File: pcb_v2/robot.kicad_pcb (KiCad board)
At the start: 2 copper layers, 34.9 x 72.4 mm, 28 parts, among them J1 M1 PWR, J11 MB CTRL, J12 MA CTRL, J2 M2 PWR, J3 Power Connector, J4 BATT, J5 TB6612_Motor_Driver, J7 PWR, Q1 2N3904, Q2 2N3904, U2 L7805, U3 L78L33_TO92

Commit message: SMB, 10 Dec 19, updated 3d print files.
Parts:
- removed the ? at (123.2, 35.6)
- added ?: , , F.Cu at (102.9, 27.9)
- added ?: , , F.Cu at (96.5, 27.9)
- added D2: LED, LED_THT:LED_D3.0mm, F.Cu at (99.1, 22.9)
- added Q3: 2N3906, Package_TO_SOT_THT:TO-92_Inline_Wide, F.Cu at (108.0, 22.9)
- added R2: 10k, Resistor_THT:R_Axial_DIN0207_L6.3mm_D2.5mm_P10.16mm_Horizontal, F.Cu at (102.9, 27.9)
- added R7: 13k, Resistor_THT:R_Axial_DIN0207_L6.3mm_D2.5mm_P10.16mm_Horizontal, F.Cu at (118.1, 27.9)
- added R8: 1k, Resistor_THT:R_Axial_DIN0207_L6.3mm_D2.5mm_P10.16mm_Horizontal, F.Cu at (118.1, 22.9)
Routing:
- net GND: track 139.6 -> 175.4 mm
- net +5V: track 96.6 -> 127.1 mm
- net Net-(D2-Pad2): track 0.00 -> 28.8 mm
- net Net-(Q3-Pad2): track 0.00 -> 11.2 mm
- net +BATT: track 74.8 -> 83.3 mm
- net Net-(Q3-Pad3): track 0.00 -> 5.08 mm
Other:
- board size 34.9 x 72.4 mm -> 34.9 x 82.5 mm
- board text added: "13k"
- board text added: "1k"
- board text added: "Beyer (c) 2019"
- board text removed: "Walchko (c) 2018"

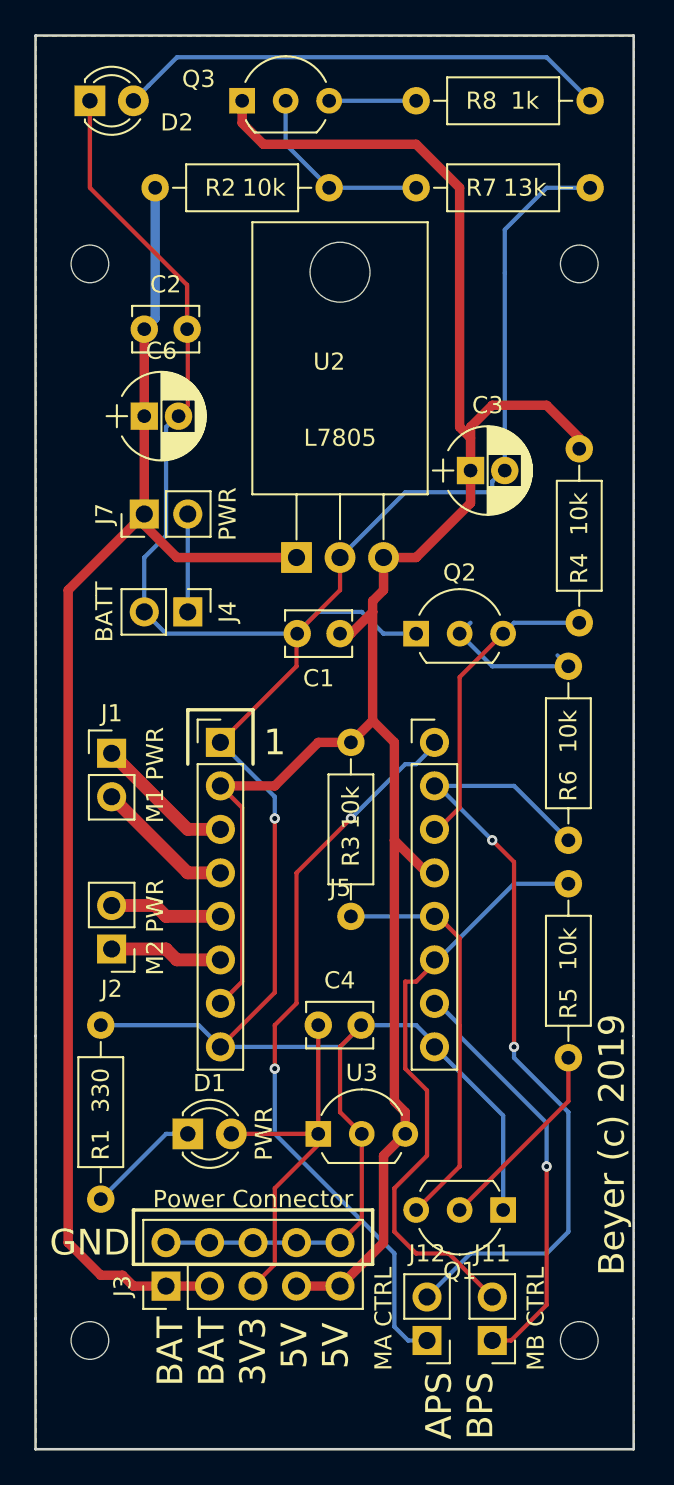
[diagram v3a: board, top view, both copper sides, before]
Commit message: SMB, 28 Apr 2020, Updated PCB v2.
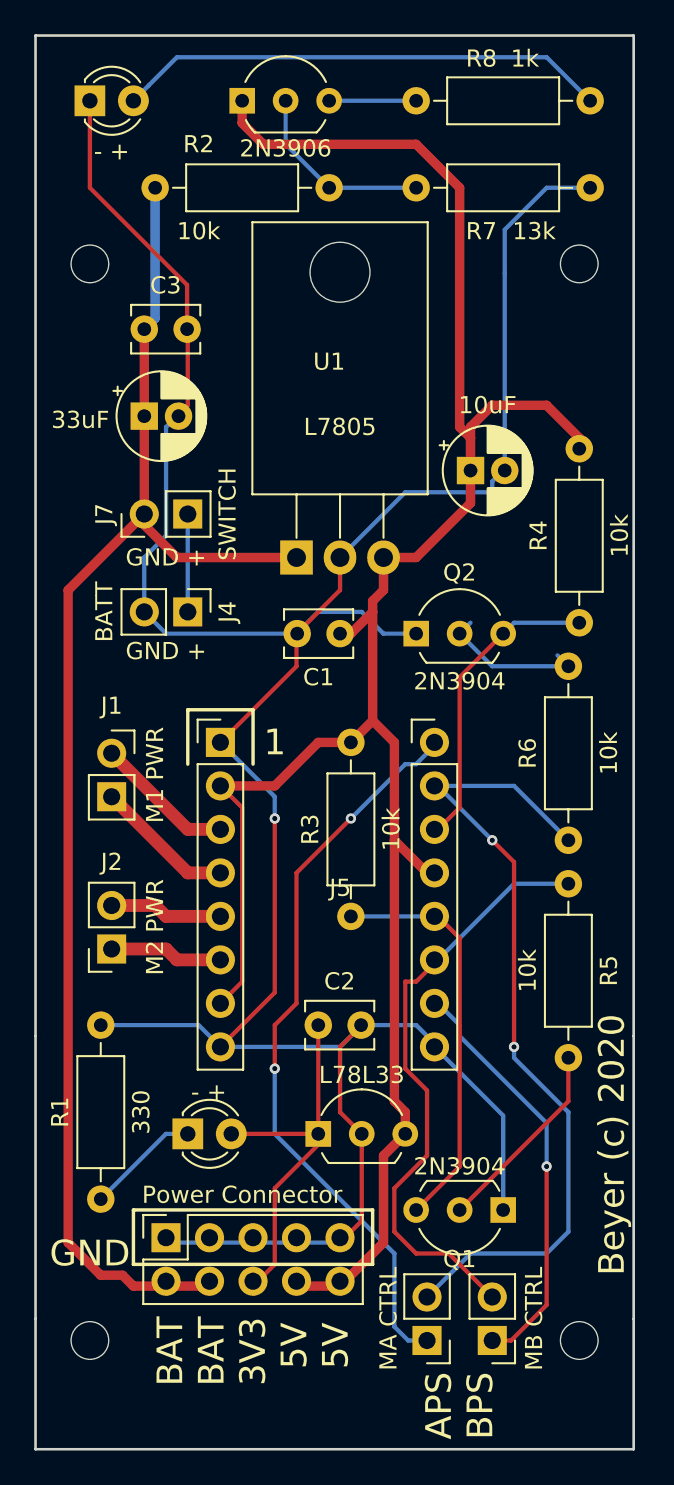
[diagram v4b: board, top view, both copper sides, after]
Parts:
- C1: footprint Capacitors_THT:C_Disc_D3.8mm_W2.6mm_P2.50mm -> Capacitor_THT:C_Disc_D3.8mm_W2.6mm_P2.50mm
- C2: renamed from C4; footprint Capacitors_THT:C_Disc_D3.8mm_W2.6mm_P2.50mm -> Capacitor_THT:C_Disc_D3.8mm_W2.6mm_P2.50mm
- C3: renamed from C2; footprint Capacitors_THT:C_Disc_D3.8mm_W2.6mm_P2.50mm -> Capacitor_THT:C_Disc_D3.8mm_W2.6mm_P2.50mm
- C4: renamed from C3; footprint Capacitors_THT:CP_Radial_D5.0mm_P2.00mm -> Capacitor_THT:CP_Radial_D5.0mm_P2.00mm
- C5: renamed from C6; footprint Capacitors_THT:CP_Radial_D5.0mm_P2.00mm -> Capacitor_THT:CP_Radial_D5.0mm_P2.00mm
- D1: value PWR -> - +; footprint LEDs:LED_D3.0mm -> LED_THT:LED_D3.0mm
- D2: value LED -> - +
- J1, J2: footprint Pin_Headers:Pin_Header_Straight_1x02_Pitch2.54mm -> Connector_PinSocket_2.54mm:PinSocket_1x02_P2.54mm_Vertical
- J11, J12, J4: footprint Pin_Headers:Pin_Header_Straight_1x02_Pitch2.54mm -> Connector_PinHeader_2.54mm:PinHeader_1x02_P2.54mm_Vertical
- J3: footprint Pin_Headers:Pin_Header_Straight_2x05_Pitch2.54mm -> Connector_PinSocket_2.54mm:PinSocket_2x05_P2.54mm_Vertical
- J7: value PWR -> SWITCH; footprint Pin_Headers:Pin_Header_Straight_1x02_Pitch2.54mm -> Connector_PinHeader_2.54mm:PinHeader_1x02_P2.54mm_Vertical
- R1, R3, R4, R5, R6: footprint Resistors_THT:R_Axial_DIN0207_L6.3mm_D2.5mm_P10.16mm_Horizontal -> Resistor_THT:R_Axial_DIN0207_L6.3mm_D2.5mm_P10.16mm_Horizontal
- U1: renamed from U2; footprint TO_SOT_Packages_THT:TO-220-3_Horizontal -> Package_TO_SOT_THT:TO-220-3_Horizontal_TabDown
- U3: value L78L33_TO92 -> L78L33
- moved J3 2.83 mm to (103.5, 89.2)
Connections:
- D2 pad 2: Net-(D2-Pad2) -> (no net)
- Q3 pad 2: Net-(Q3-Pad2) -> (no net)
- Q3 pad 3: Net-(Q3-Pad3) -> (no net)
- R2 pad 1: +BATT -> (no net)
- R2 pad 2: Net-(Q3-Pad2) -> (no net)
- R7 pad 1: Net-(Q3-Pad2) -> (no net)
- R7 pad 2: GND -> (no net)
- R8 pad 1: Net-(Q3-Pad3) -> (no net)
- R8 pad 2: Net-(D2-Pad2) -> (no net)
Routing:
- net (no net): track 0.00 -> 45.1 mm
- net Net-(D2-Pad2): track 28.8 -> 0.00 mm
- net Net-(Q3-Pad2): track 11.2 -> 0.00 mm
- net Net-(Q3-Pad3): track 5.08 -> 0.00 mm
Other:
- board text added: "Beyer (c) 2020"
- board text removed: "13k"
- board text removed: "1k"
- board text removed: "Beyer (c) 2019"
